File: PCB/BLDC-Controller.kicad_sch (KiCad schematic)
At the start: 79 parts, among them J1 Phase_A, J2 Phase_B, J3 Phase_C, J4 Prog, J5 Receiver, J6 Bat_In, Q1 P75NF75, Q2 P75NF75, Q3 P75NF75, Q4 P75NF75, Q5 P75NF75, Q6 P75NF75, SW1 RST, SW2 Speed+, SW3 Speed-, U1 UCC27282, U2 UCC27282, U3 UCC27282, U4 ATmega328P-P, U5 LM7805, U6 LM317, Y1 16M

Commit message: Updated schematic. Added new documentation.
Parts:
- C17: now not fitted
- R11: renamed from R8; value 33k -> 47k
- R12: renamed from R9; value 33k -> 47k
- R13: renamed from R10; value 33k -> 47k
- R17: renamed from R14; value 33k -> 47k
- R18: renamed from R15; value 33k -> 47k
- R19: renamed from R16; value 33k -> 47k
- renumbered C20 to C19, C21 to C20, C23 to C21, C24 to C22, C25 to C23, C19 to C24, C22 to C25, D7 to D6, D8 to D7, D6 to D8, R19 to R10, R11 to R14, R12 to R15, R13 to R16, R17 to R8, R18 to R9, U6 to U5, U5 to U6
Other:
- note removed: "Max voltage (25.2V input) = 4.75V"
- moved on the sheet: C10, C11, C12, C13, C14, C15, C18, D1, D3, D5, H1, H2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

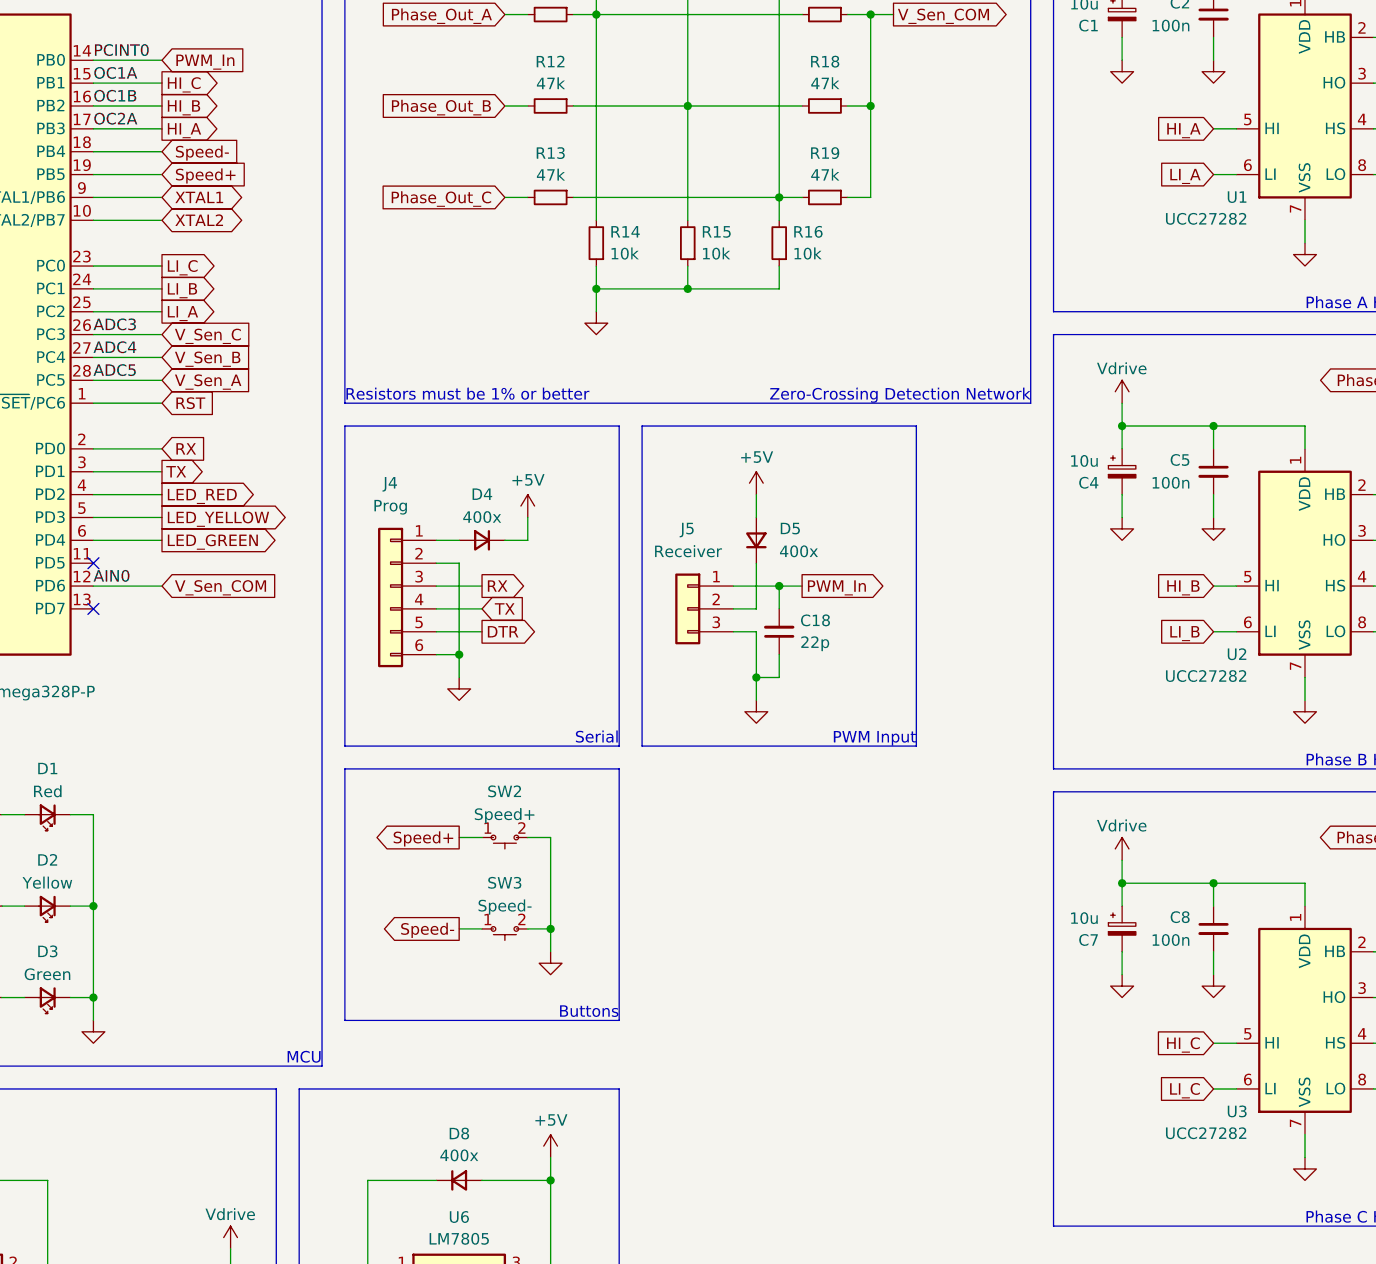
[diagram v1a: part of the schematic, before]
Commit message: Added new images. Modified schematic and PCB.
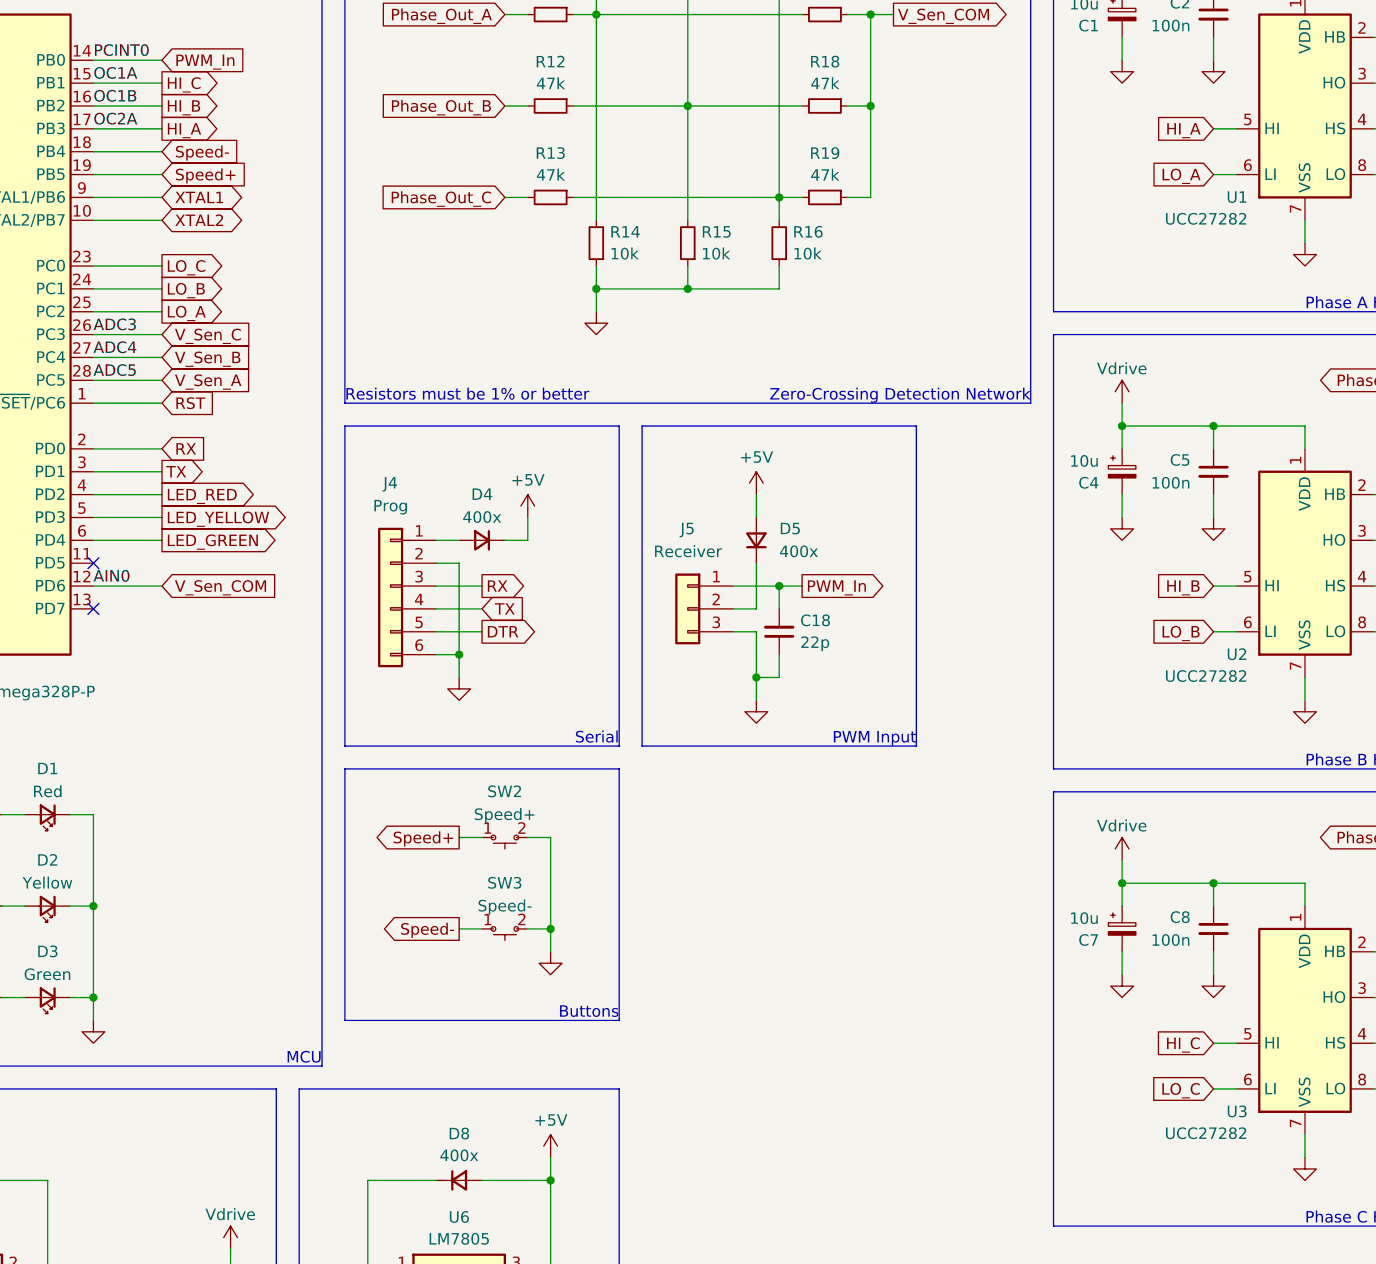
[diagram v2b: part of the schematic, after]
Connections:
- net LI_A renamed LO_A
- net LI_B renamed LO_B
- net LI_C renamed LO_C
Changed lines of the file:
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@@
     )
   )
-  (global_label "LI_B" (shape output) (at 93.98 58.42 0) (fields_autoplaced)
+  (global_label "LO_B" (shape output) (at 93.98 58.42 0) (fields_autoplaced)
     (effects (font (size 1.27 1.27)) (justify left))
     (property "Intersheetrefs" "${INTERSHEET_REFS}" (at 100.8357 58.42 0)
@@
     )
   )
-  (global_label "LI_A" (shape input) (at 210.82 45.72 180) (fields_autoplaced)
+  (global_label "LO_A" (shape input) (at 210.82 45.72 180) (fields_autoplaced)
     (effects (font (size 1.27 1.27)) (justify right))
     (property "Intersheetrefs" "${INTERSHEET_REFS}" (at 204.1457 45.72 0)
@@
     )
   )
-  (global_label "LI_C" (shape input) (at 210.82 147.32 180) (fields_autoplaced)
+  (global_label "LO_C" (shape input) (at 210.82 147.32 180) (fields_autoplaced)
     (effects (font (size 1.27 1.27)) (justify right))
     (property "Intersheetrefs" "${INTERSHEET_REFS}" (at 203.9643 147.32 0)
@@
     )
   )
-  (global_label "LI_B" (shape input) (at 210.82 96.52 180) (fields_autoplaced)
+  (global_label "LO_B" (shape input) (at 210.82 96.52 180) (fields_autoplaced)
     (effects (font (size 1.27 1.27)) (justify right))
     (property "Intersheetrefs" "${INTERSHEET_REFS}" (at 203.9643 96.52 0)
@@
     )
   )
-  (global_label "LI_A" (shape output) (at 93.98 60.96 0) (fields_autoplaced)
+  (global_label "LO_A" (shape output) (at 93.98 60.96 0) (fields_autoplaced)
     (effects (font (size 1.27 1.27)) (justify left))
     (property "Intersheetrefs" "${INTERSHEET_REFS}" (at 100.6543 60.96 0)
@@
     )
   )
-  (global_label "LI_C" (shape output) (at 93.98 55.88 0) (fields_autoplaced)
+  (global_label "LO_C" (shape output) (at 93.98 55.88 0) (fields_autoplaced)
     (effects (font (size 1.27 1.27)) (justify left))
     (property "Intersheetrefs" "${INTERSHEET_REFS}" (at 100.8357 55.88 0)

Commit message: Removed extraneous details.
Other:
- company: Aria Tso -> Ariamelon
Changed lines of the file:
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@@
     (date "2024-04-08")
     (rev "V1.1")
-    (company "Aria Tso")
-    (comment 1 "University of Brighton")
-    (comment 2 "School of Architecture, Technology and Engineering")
+    (company "Ariamelon")
+    (comment 1 "https://github.com/Ariamelon/BLDC-Controller/")
   )
   (junction (at 86.36 137.16) (diameter 0) (color 0 0 0 0)
